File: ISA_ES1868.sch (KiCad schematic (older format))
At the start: 14 parts, among them J1 ISA BUS

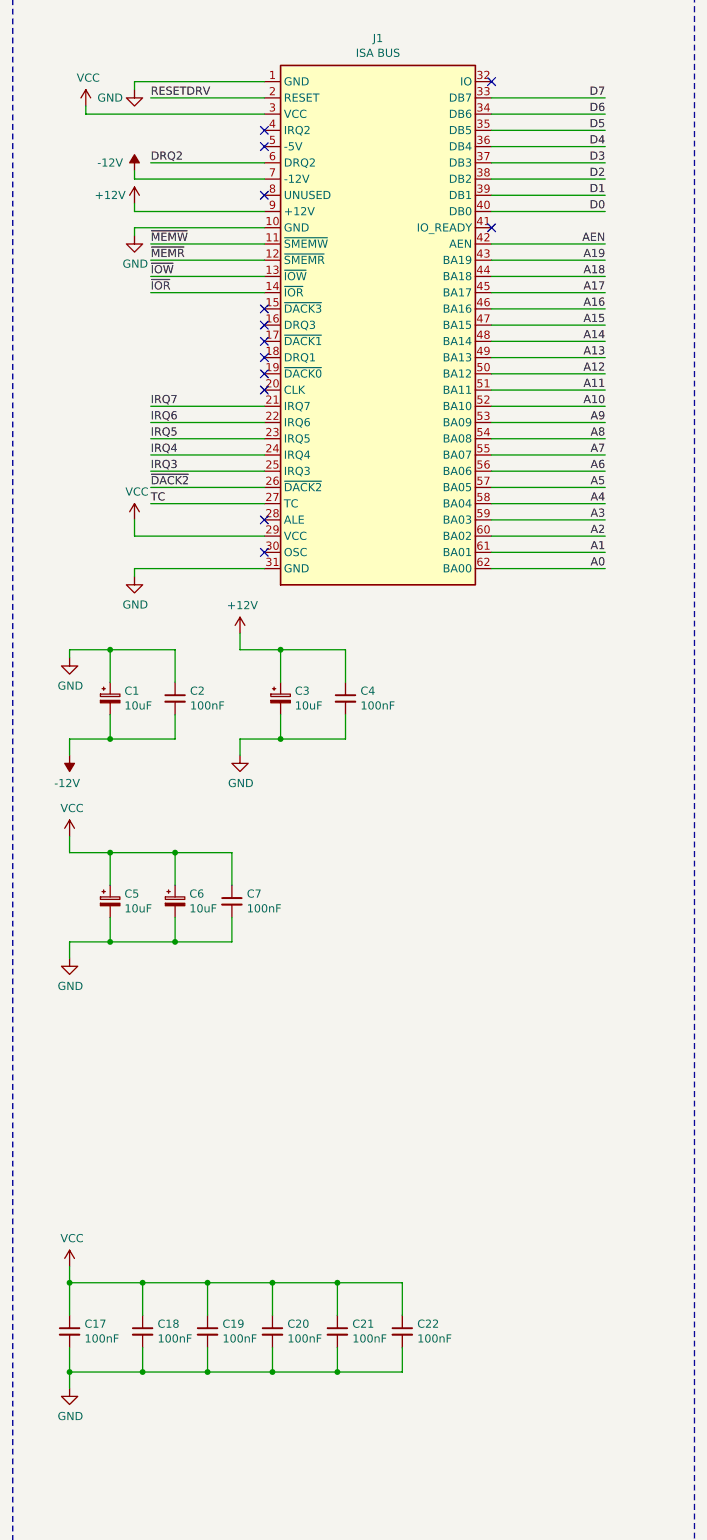
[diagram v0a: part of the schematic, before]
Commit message: Remove some unused connections from edge
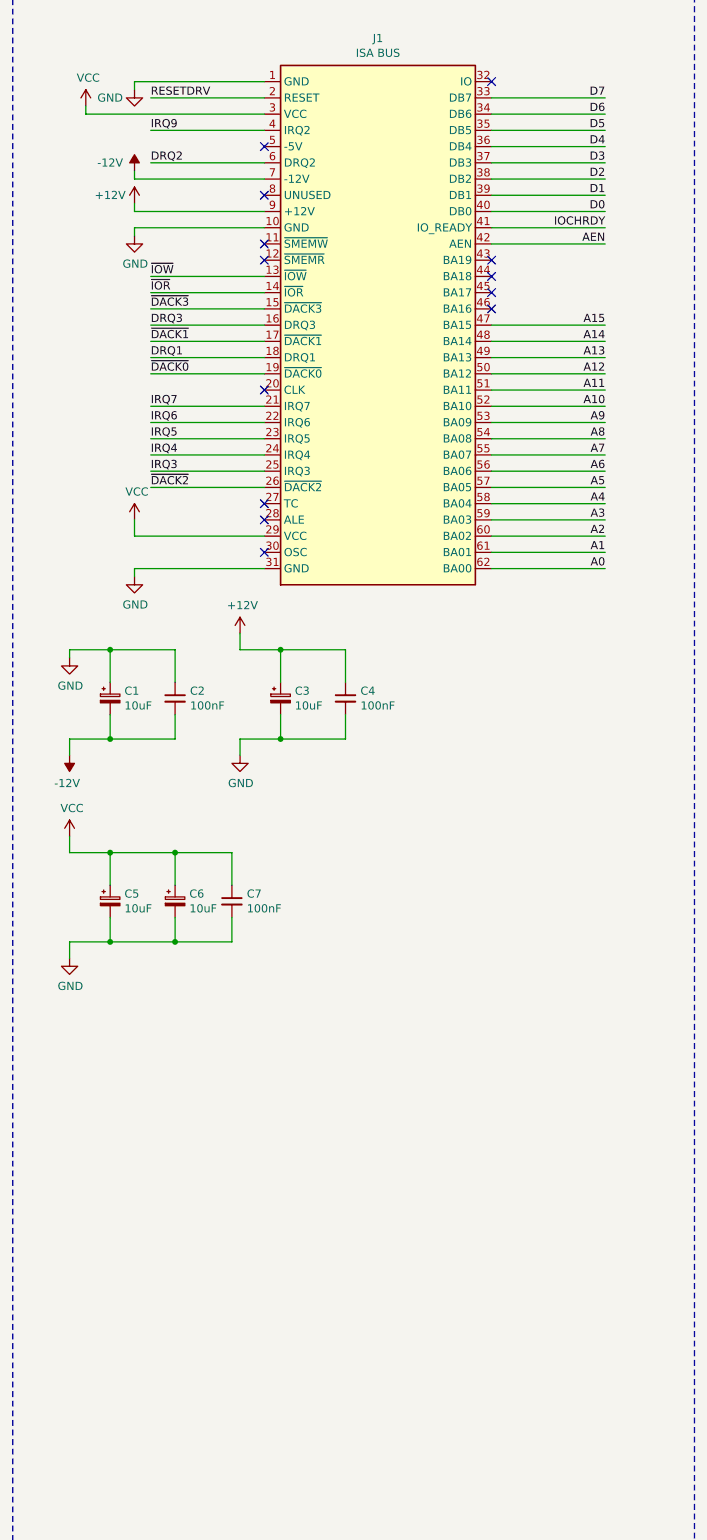
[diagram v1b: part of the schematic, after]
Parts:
- removed C17, C18, C19, C20, C21, C22: 100nF, Capacitor_THT:C_Disc_D6.0mm_W2.5mm_P5.00mm, symbol Device:C_Small
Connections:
- net ~DACK3: now reaches J1.15 (~DACK3)
- net DRQ3: now reaches J1.16 (DRQ3)
- net ~DACK1: now reaches J1.17 (~DACK1)
- net DRQ1: now reaches J1.18 (DRQ1)
- net ~DACK0: now reaches J1.19 (~DACK0)
- net IRQ9: now reaches J1.4 (IRQ2)
- net IOCHRDY: now reaches J1.41 (IO_READY)
- net A16: no longer names the net of J1.46 (BA16)
- net A17: no longer names the net of J1.45 (BA17)
- net A18: no longer names the net of J1.44 (BA18)
- net A19: no longer names the net of J1.43 (BA19)
- net TC: no longer names the net of J1.27 (TC)
- net ~MEMR: no longer names the net of J1.12 (~SMEMR)
- net ~MEMW: no longer names the net of J1.11 (~SMEMW)
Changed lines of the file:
@@
 	2300 6950 1600 6950
 Wire Wire Line
-	2300 7450 1600 7450
-Wire Wire Line
-	2300 7550 1600 7550
-Wire Wire Line
 	2300 7650 1600 7650
 Wire Wire Line
@@
 	2300 8850 1600 8850
 Wire Wire Line
-	2300 8950 1600 8950
-Wire Wire Line
-	2300 9050 1600 9050
-Wire Wire Line
 	4400 6550 3700 6550
 Wire Wire Line
@@
 	4400 7450 3700 7450
 Wire Wire Line
-	4400 7550 3700 7550
-Wire Wire Line
-	4400 7650 3700 7650
-Wire Wire Line
-	4400 7750 3700 7750
-Wire Wire Line
-	4400 7850 3700 7850
-Wire Wire Line
 	4400 7950 3700 7950
 Wire Wire Line
@@
 Wire Wire Line
 	4400 9450 3700 9450
-NoConn ~ 2300 6750
 NoConn ~ 2300 6850
 NoConn ~ 2300 7150
-NoConn ~ 2300 7850
-NoConn ~ 2300 7950
-NoConn ~ 2300 8050
-NoConn ~ 2300 8150
-NoConn ~ 2300 8250
 NoConn ~ 2300 8350
 NoConn ~ 2300 9150
 NoConn ~ 2300 9350
-NoConn ~ 3700 7350
 NoConn ~ 3700 6450
 Text Label 4400 9450 2    50   ~ 0
@@
 Text Label 4400 7950 2    50   ~ 0
 A15
-Text Label 4400 7850 2    50   ~ 0
-A16
-Text Label 4400 7750 2    50   ~ 0
-A17
-Text Label 4400 7650 2    50   ~ 0
-A18
-Text Label 4400 7550 2    50   ~ 0
-A19
 Text Label 4400 7450 2    50   ~ 0
 AEN
@@
 Wire Wire Line
 	1500 7350 2300 7350
-Text Label 1600 7450 0    50   ~ 0
-~MEMW
-Text Label 1600 7550 0    50   ~ 0
-~MEMR
 Text Label 1600 7650 0    50   ~ 0
 ~IOW
@@
 Text Label 1600 8950 0    50   ~ 0
 ~DACK2
-Text Label 1600 9050 0    50   ~ 0
-TC
 $Comp
 L power:GND #PWR0132
@@
 Text Notes 900  15700 0    197  ~ 0
 ISA & Decoupling
-$Comp
-L power:GND #PWR0126
-U 1 1 614742DA
-P 1100 14500
-F 0 "#PWR0126" H 1100 14250 50  0001 C CNN
-F 1 "GND" H 1105 14327 50  0000 C CNN
-F 2 "" H 1100 14500 50  0001 C CNN
-F 3 "" H 1100 14500 50  0001 C CNN
-	1    1100 14500
-	1    0    0    -1
-$EndComp
-Wire Wire Line
-	1100 14400 1100 14500
-Wire Wire Line
-	1100 13750 1100 13850
-$Comp
-L power:VCC #PWR0145
-U 1 1 614742E6
-P 1100 13750
-F 0 "#PWR0145" H 1100 13600 50  0001 C CNN
-F 1 "VCC" H 1115 13923 50  0000 C CNN
-F 2 "" H 1100 13750 50  0001 C CNN
-F 3 "" H 1100 13750 50  0001 C CNN
-	1    1100 13750
-	1    0    0    -1
-$EndComp
-$Comp
-L Device:C_Small C17
-U 1 1 663DB2E1
-P 1100 14150
-F 0 "C17" H 1192 14196 50  0000 L CNN
-F 1 "100nF" H 1192 14105 50  0000 L CNN
-F 2 "Capacitor_THT:C_Disc_D6.0mm_W2.5mm_P5.00mm" H 1100 14150 50  0001 C CNN
-F 3 "~" H 1100 14150 50  0001 C CNN
-	1    1100 14150
-	1    0    0    -1
-$EndComp
-$Comp
-L Device:C_Small C18
-U 1 1 663DCDF9
-P 1550 14150
-F 0 "C18" H 1642 14196 50  0000 L CNN
-F 1 "100nF" H 1642 14105 50  0000 L CNN
-F 2 "Capacitor_THT:C_Disc_D6.0mm_W2.5mm_P5.00mm" H 1550 14150 50  0001 C CNN
-F 3 "~" H 1550 14150 50  0001 C CNN
-	1    1550 14150
-	1    0    0    -1
-$EndComp
-Wire Wire Line
-	1550 13850 1550 14050
-Wire Wire Line
-	1550 14400 1550 14250
-Wire Wire Line
-	1100 14050 1100 13850
-Wire Wire Line
-	1100 14250 1100 14400
-$Comp
-L Device:C_Small C19
-U 1 1 67C001EA
-P 1950 14150
-F 0 "C19" H 2042 14196 50  0000 L CNN
-F 1 "100nF" H 2042 14105 50  0000 L CNN
-F 2 "Capacitor_THT:C_Disc_D6.0mm_W2.5mm_P5.00mm" H 1950 14150 50  0001 C CNN
-F 3 "~" H 1950 14150 50  0001 C CNN
-	1    1950 14150
-	1    0    0    -1
-$EndComp
-$Comp
-L Device:C_Small C20
-U 1 1 67C051F6
-P 2350 14150
-F 0 "C20" H 2442 14196 50  0000 L CNN
-F 1 "100nF" H 2442 14105 50  0000 L CNN
-F 2 "Capacitor_THT:C_Disc_D6.0mm_W2.5mm_P5.00mm" H 2350 14150 50  0001 C CNN
-F 3 "~" H 2350 14150 50  0001 C CNN
-	1    2350 14150
-	1    0    0    -1
-$EndComp
-Wire Wire Line
-	2350 13850 2350 14050
-Wire Wire Line
-	2350 14250 2350 14400
-Wire Wire Line
-	1950 14050 1950 13850
-Wire Wire Line
-	1950 14250 1950 14400
-$Comp
-L Device:C_Small C21
-U 1 1 61A4282F
-P 2750 14150
-F 0 "C21" H 2842 14196 50  0000 L CNN
-F 1 "100nF" H 2842 14105 50  0000 L CNN
-F 2 "Capacitor_THT:C_Disc_D6.0mm_W2.5mm_P5.00mm" H 2750 14150 50  0001 C CNN
-F 3 "~" H 2750 14150 50  0001 C CNN
-	1    2750 14150
-	1    0    0    -1
-$EndComp
-Wire Wire Line
-	2750 13850 2750 14050
-Wire Wire Line
-	2750 14400 2750 14250
-$Comp
-L Device:C_Small C22
-U 1 1 6730EDE6
-P 3150 14150
-F 0 "C22" H 3242 14196 50  0000 L CNN
-F 1 "100nF" H 3242 14105 50  0000 L CNN
-F 2 "Capacitor_THT:C_Disc_D6.0mm_W2.5mm_P5.00mm" H 3150 14150 50  0001 C CNN
-F 3 "~" H 3150 14150 50  0001 C CNN
-	1    3150 14150
-	1    0    0    -1
-$EndComp
-Wire Wire Line
-	3150 13850 3150 14050
-Wire Wire Line
-	3150 14250 3150 14400
-Wire Wire Line
-	1100 14400 1550 14400
-Wire Wire Line
-	1100 13850 1550 13850
-Connection ~ 1100 13850
-Connection ~ 1100 14400
-Connection ~ 1550 13850
-Wire Wire Line
-	1550 13850 1950 13850
-Connection ~ 1550 14400
-Wire Wire Line
-	1550 14400 1950 14400
-Connection ~ 1950 13850
-Connection ~ 1950 14400
-Connection ~ 2350 13850
-Connection ~ 2350 14400
-Connection ~ 2750 13850
-Connection ~ 2750 14400
-Wire Wire Line
-	1950 13850 2350 13850
-Wire Wire Line
-	2350 13850 2750 13850
-Wire Wire Line
-	1950 14400 2350 14400
-Wire Wire Line
-	2350 14400 2750 14400
-Wire Wire Line
-	2750 13850 3150 13850
-Wire Wire Line
-	2750 14400 3150 14400
+NoConn ~ 2300 9050
+Wire Wire Line
+	2300 8950 1600 8950
+Text Label 1600 7850 0    50   ~ 0
+~DACK3
+Wire Wire Line
+	2300 7850 1600 7850
+Text Label 1600 8050 0    50   ~ 0
+~DACK1
+Wire Wire Line
+	2300 8050 1600 8050
+Text Label 1600 8250 0    50   ~ 0
+~DACK0
+Wire Wire Line
+	2300 8250 1600 8250
+Wire Wire Line
+	2300 8150 1600 8150
+Text Label 1600 8150 0    50   ~ 0
+DRQ1
+Wire Wire Line
+	2300 7950 1600 7950
+Text Label 1600 7950 0    50   ~ 0
+DRQ3
+Wire Wire Line
+	2300 6750 1600 6750
+Text Label 1600 6750 0    50   ~ 0
+IRQ9
+NoConn ~ 2300 7450
+NoConn ~ 2300 7550
+NoConn ~ 3700 7550
+NoConn ~ 3700 7650
+NoConn ~ 3700 7750
+NoConn ~ 3700 7850
+Wire Wire Line
+	3700 7350 4400 7350
+Text Label 4400 7350 2    50   ~ 0
+IOCHRDY
 $EndSCHEMATC

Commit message: Begin drawing schematic
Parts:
- added C12: 10uF, Capacitor_THT:CP_Radial_D5.0mm_P2.50mm, symbol Device:CP_Small
- added C4, C5: 100nF, Capacitor_THT:C_Disc_D6.0mm_W2.5mm_P5.00mm, symbol Device:C_Small
- added U1: L78L05_TO92, Package_TO_SOT_THT:TO-92_Inline, symbol Regulator_Linear:L78L05_TO92
- added U4: 93LC66, symbol Memory_EEPROM:93CxxC
- added U?: ES1868F, symbol custom_components:ES1868F
- renumbered C1 to C?, C2 to C?, C3 to C?, C4 to C?, C5 to C?, C7 to C?, C6 to C?
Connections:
- net +12V: now also C4.1, U1.3 (VI)
- net GND: now also U?.24 (GND), U?.52 (GND), U?.60 (GND), U?.7 (GND), U?.77 (GND)
- net VCC: now also U?.26 (VCC), U?.3 (VCC), U?.57 (VCC), U?.80 (VCC)
- new net: C12.1, C5.1, U1.1 (VO), U?.43 (VDDA)
- new net GNDA: C12.2, C4.2, C5.2, U1.2 (GND), U?.41 (GNDA)
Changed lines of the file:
@@
 	1500 9250 2300 9250
 $Comp
-L Device:CP_Small C1
+L Device:CP_Small C?
 U 1 1 610853FE
 P 1350 10250
-F 0 "C1" H 1438 10296 50  0000 L CNN
+F 0 "C?" H 1438 10296 50  0000 L CNN
 F 1 "10uF" H 1438 10205 50  0000 L CNN
 F 2 "Capacitor_THT:CP_Radial_D5.0mm_P2.50mm" H 1350 10250 50  0001 C CNN
@@
 $EndComp
 $Comp
-L Device:C_Small C2
+L Device:C_Small C?
 U 1 1 61086024
 P 1750 10250
-F 0 "C2" H 1842 10296 50  0000 L CNN
+F 0 "C?" H 1842 10296 50  0000 L CNN
 F 1 "100nF" H 1842 10205 50  0000 L CNN
 F 2 "Capacitor_THT:C_Disc_D6.0mm_W2.5mm_P5.00mm" H 1750 10250 50  0001 C CNN
@@
 Connection ~ 1350 10500
 $Comp
-L Device:CP_Small C3
+L Device:CP_Small C?
 U 1 1 6116AF87
 P 2400 10250
-F 0 "C3" H 2488 10296 50  0000 L CNN
+F 0 "C?" H 2488 10296 50  0000 L CNN
 F 1 "10uF" H 2488 10205 50  0000 L CNN
 F 2 "Capacitor_THT:CP_Radial_D5.0mm_P2.50mm" H 2400 10250 50  0001 C CNN
@@
 $EndComp
 $Comp
-L Device:C_Small C4
+L Device:C_Small C?
 U 1 1 6116B0B7
 P 2800 10250
-F 0 "C4" H 2892 10296 50  0000 L CNN
+F 0 "C?" H 2892 10296 50  0000 L CNN
 F 1 "100nF" H 2892 10205 50  0000 L CNN
 F 2 "Capacitor_THT:C_Disc_D6.0mm_W2.5mm_P5.00mm" H 2800 10250 50  0001 C CNN
@@
 $EndComp
 $Comp
-L Device:CP_Small C5
+L Device:CP_Small C?
 U 1 1 61243061
 P 1350 11500
-F 0 "C5" H 1438 11546 50  0000 L CNN
+F 0 "C?" H 1438 11546 50  0000 L CNN
 F 1 "10uF" H 1438 11455 50  0000 L CNN
 F 2 "Capacitor_THT:CP_Radial_D5.0mm_P2.50mm" H 1350 11500 50  0001 C CNN
@@
 $EndComp
 $Comp
-L Device:C_Small C7
+L Device:C_Small C?
 U 1 1 612431D5
 P 2100 11500
-F 0 "C7" H 2192 11546 50  0000 L CNN
+F 0 "C?" H 2192 11546 50  0000 L CNN
 F 1 "100nF" H 2192 11455 50  0000 L CNN
 F 2 "Capacitor_THT:C_Disc_D6.0mm_W2.5mm_P5.00mm" H 2100 11500 50  0001 C CNN
@@
 $EndComp
 $Comp
-L Device:CP_Small C6
+L Device:CP_Small C?
 U 1 1 612911A6
 P 1750 11500
-F 0 "C6" H 1838 11546 50  0000 L CNN
+F 0 "C?" H 1838 11546 50  0000 L CNN
 F 1 "10uF" H 1838 11455 50  0000 L CNN
 F 2 "Capacitor_THT:CP_Radial_D5.0mm_P2.50mm" H 1750 11500 50  0001 C CNN
@@
 Text Label 4400 7350 2    50   ~ 0
 IOCHRDY
+$Comp
+L Memory_EEPROM:93CxxC U4
+U 1 1 60AA3033
+P 16100 8200
+F 0 "U4" H 15850 8450 50  0000 C CNN
+F 1 "93LC66" H 16300 8450 50  0000 C CNN
+F 2 "" H 16100 8200 50  0001 C CNN
+F 3 "http://ww1.microchip.com/downloads/en/DeviceDoc/20001749K.pdf" H 16100 8200 50  0001 C CNN
+	1    16100 8200
+	1    0    0    -1
+$EndComp
+$Comp
+L power:VCC #PWR?
+U 1 1 60AA4053
+P 11850 4000
+F 0 "#PWR?" H 11850 3850 50  0001 C CNN
+F 1 "VCC" H 11865 4173 50  0000 C CNN
+F 2 "" H 11850 4000 50  0001 C CNN
+F 3 "" H 11850 4000 50  0001 C CNN
+	1    11850 4000
+	1    0    0    -1
+$EndComp
+Wire Wire Line
+	11700 4200 11700 4100
+Wire Wire Line
+	11700 4100 11800 4100
+Wire Wire Line
+	12000 4100 12000 4200
+Wire Wire Line
+	11900 4200 11900 4100
+Connection ~ 11900 4100
+Wire Wire Line
+	11900 4100 12000 4100
+Wire Wire Line
+	11800 4200 11800 4100
+Connection ~ 11800 4100
+Wire Wire Line
+	11800 4100 11850 4100
+Wire Wire Line
+	11850 4100 11850 4000
+Connection ~ 11850 4100
+Wire Wire Line
+	11850 4100 11900 4100
+$Comp
+L power:GND #PWR?
+U 1 1 60AB4414
+P 12000 10700
+F 0 "#PWR?" H 12000 10450 50  0001 C CNN
+F 1 "GND" H 12005 10527 50  0000 C CNN
+F 2 "" H 12000 10700 50  0001 C CNN
+F 3 "" H 12000 10700 50  0001 C CNN
+	1    12000 10700
+	1    0    0    -1
+$EndComp
+Wire Wire Line
+	11800 10500 11800 10600
+Wire Wire Line
+	11800 10600 11900 10600
+Wire Wire Line
+	12200 10600 12200 10500
+Wire Wire Line
+	12100 10500 12100 10600
+Connection ~ 12100 10600
+Wire Wire Line
+	12100 10600 12200 10600
+Wire Wire Line
+	12000 10500 12000 10600
+Connection ~ 12000 10600
+Wire Wire Line
+	12000 10600 12100 10600
+Wire Wire Line
+	12000 10600 12000 10700
+Wire Wire Line
+	11900 10500 11900 10600
+Connection ~ 11900 10600
+Wire Wire Line
+	11900 10600 12000 10600
+$Comp
+L power:GNDA #PWR?
+U 1 1 60AC576E
+P 13100 4800
+F 0 "#PWR?" H 13100 4550 50  0001 C CNN
+F 1 "GNDA" H 13250 4750 50  0000 C CNN
+F 2 "" H 13100 4800 50  0001 C CNN
+F 3 "" H 13100 4800 50  0001 C CNN
+	1    13100 4800
+	1    0    0    -1
+$EndComp
+Wire Wire Line
+	12450 4750 12700 4750
+Wire Wire Line
+	13100 4750 13100 4800
+Wire Wire Line
+	12650 4050 12650 4100
+Connection ~ 12650 4050
+Wire Wire Line
+	13300 4050 13300 4000
+Wire Wire Line
+	12650 4050 13300 4050
+Wire Wire Line
+	12650 4000 12650 4050
+$Comp
+L power:GNDA #PWR?
+U 1 1 60AE9C0E
+P 12650 4100
+F 0 "#PWR?" H 12650 3850 50  0001 C CNN
+F 1 "GNDA" H 12800 4050 50  0000 C CNN
+F 2 "" H 12650 4100 50  0001 C CNN
+F 3 "" H 12650 4100 50  0001 C CNN
+	1    12650 4100
+	1    0    0    -1
+$EndComp
+Wire Wire Line
+	12650 3700 13000 3700
+Connection ~ 12650 3700
+Wire Wire Line
+	12650 3700 12650 3800
+Wire Wire Line
+	12400 3700 12650 3700
+Wire Wire Line
+	12400 3650 12400 3700
+$Comp
+L power:+12V #PWR?
+U 1 1 60AD7461
+P 12400 3650
+F 0 "#PWR?" H 12400 3500 50  0001 C CNN
+F 1 "+12V" H 12250 3700 50  0000 C CNN
+F 2 "" H 12400 3650 50  0001 C CNN
+F 3 "" H 12400 3650 50  0001 C CNN
+	1    12400 3650
+	1    0    0    -1
+$EndComp
+$Comp
+L Device:C_Small C4
+U 1 1 60ACF5FB
+P 12650 3900
+F 0 "C4" H 12742 3946 50  0000 L CNN
+F 1 "100nF" H 12742 3855 50  0000 L CNN
+F 2 "Capacitor_THT:C_Disc_D6.0mm_W2.5mm_P5.00mm" H 12650 3900 50  0001 C CNN
+F 3 "~" H 12650 3900 50  0001 C CNN
+	1    12650 3900
+	1    0    0    -1
+$EndComp
+$Comp
+L Regulator_Linear:L78L05_TO92 U1
+U 1 1 60ACA4DD
+P 13300 3700
+F 0 "U1" H 13300 3942 50  0000 C CNN
+F 1 "L78L05_TO92" H 13300 3851 50  0000 C CNN
+F 2 "Package_TO_SOT_THT:TO-92_Inline" H 13300 3925 50  0001 C CIN
+F 3 "http://www.st.com/content/ccc/resource/technical/document/datasheet/15/55/e5/aa/23/5b/43/fd/CD00000446.pdf/files/CD00000446.pdf/jcr:content/translations/en.CD00000446.pdf" H 13300 3650 50  0001 C CNN
+	1    13300 3700
+	1    0    0    -1
+$EndComp
+$Comp
+L custom_components:ES1868F U?
+U 1 1 60A9AA6E
+P 11850 7150
+F 0 "U?" H 11400 10050 50  0000 C CNN
+F 1 "ES1868F" H 12200 10050 50  0000 C CNN
+F 2 "" H 11850 8100 50  0001 C CNN
+F 3 "" H 11850 8100 50  0001 C CNN
+	1    11850 7150
+	1    0    0    -1
+$EndComp
+Wire Wire Line
+	12450 4550 12700 4550
+Wire Wire Line
+	13700 4550 13700 3700
+Wire Wire Line
+	13700 3700 13600 3700
+$Comp
+L Device:C_Small C5
+U 1 1 60B0AF1F
+P 12700 4650
+F 0 "C5" H 12792 4696 50  0000 L CNN
+F 1 "100nF" H 12792 4605 50  0000 L CNN
+F 2 "Capacitor_THT:C_Disc_D6.0mm_W2.5mm_P5.00mm" H 12700 4650 50  0001 C CNN
+F 3 "~" H 12700 4650 50  0001 C CNN
+	1    12700 4650
+	1    0    0    -1
+$EndComp
+Connection ~ 12700 4550
+Wire Wire Line
+	12700 4550 13150 4550
+Connection ~ 12700 4750
+Wire Wire Line
+	12700 4750 13100 4750
+$Comp
+L Device:CP_Small C12
+U 1 1 60B0B703
+P 13150 4650
+F 0 "C12" H 13238 4696 50  0000 L CNN
+F 1 "10uF" H 13238 4605 50  0000 L CNN
+F 2 "Capacitor_THT:CP_Radial_D5.0mm_P2.50mm" H 13150 4650 50  0001 C CNN
+F 3 "~" H 13150 4650 50  0001 C CNN
+	1    13150 4650
+	1    0    0    -1
+$EndComp
+Connection ~ 13150 4550
+Wire Wire Line
+	13150 4550 13700 4550
+Wire Wire Line
+	13100 4750 13150 4750
+Connection ~ 13100 4750
 $EndSCHEMATC
